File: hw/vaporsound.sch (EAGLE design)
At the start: 80 parts, among them Q1 BSS138, Q2 BSS138, X1 MSTBV2, X2 MSTBV2, X3 MSTBV2

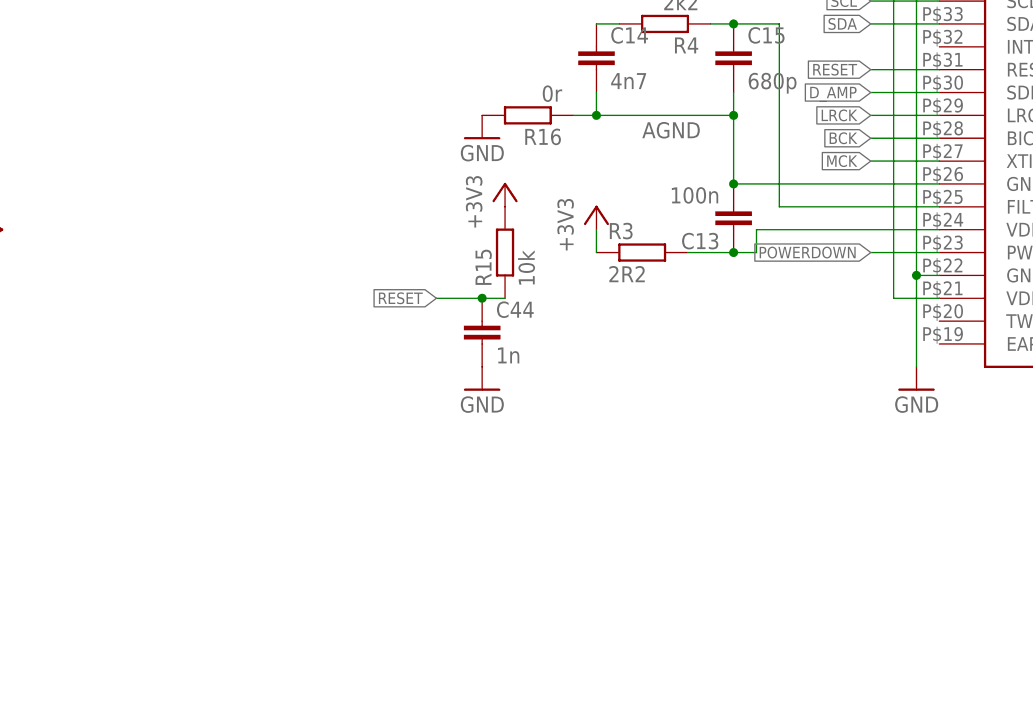
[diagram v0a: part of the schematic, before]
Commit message: Add pullup and pulldown STA350BW + minor layout fixes
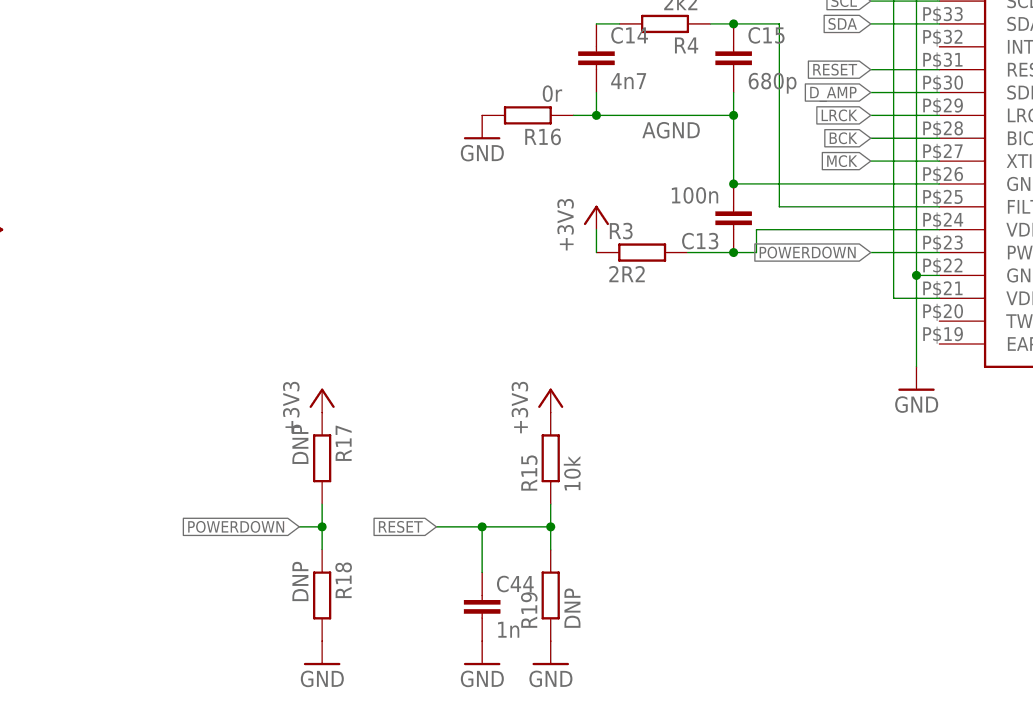
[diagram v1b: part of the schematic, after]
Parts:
- added R17, R18, R19: DNP, rcl:R-EU_R0603
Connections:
- net +3V3: now also R17.1
- net GND: now also R18.2, R19.1
- net POWERDOWN: now also R17.2, R18.1
- net RESET: now also R19.2
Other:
- moved on the sheet: C44, R15
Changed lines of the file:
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@@
 <?xml version="1.0" encoding="utf-8"?>
 <!DOCTYPE eagle SYSTEM "eagle.dtd">
-<eagle version="7.2.0">
+<eagle version="6.6.0">
 <drawing>
 <settings>
@@
 <part name="GND15" library="supply1" deviceset="GND" device=""/>
 <part name="L7" library="rcl" deviceset="R-EU_" device="R0805"/>
+<part name="R17" library="rcl" deviceset="R-EU_" device="R0603" value="DNP"/>
+<part name="R18" library="rcl" deviceset="R-EU_" device="R0603" value="DNP"/>
+<part name="+3V17" library="supply1" deviceset="+3V3" device=""/>
+<part name="GND17" library="supply1" deviceset="GND" device=""/>
+<part name="R19" library="rcl" deviceset="R-EU_" device="R0603" value="DNP"/>
+<part name="GND44" library="supply1" deviceset="GND" device=""/>
 </parts>
 <sheets>
@@
 <instance part="C42" gate="G$1" x="172.72" y="81.28"/>
 <instance part="C43" gate="G$1" x="165.1" y="81.28"/>
-<instance part="R15" gate="G$1" x="142.24" y="33.02" rot="R90"/>
-<instance part="+3V15" gate="G$1" x="142.24" y="40.64"/>
-<instance part="C44" gate="G$1" x="139.7" y="25.4"/>
-<instance part="GND40" gate="1" x="139.7" y="17.78" rot="MR0"/>
+<instance part="R15" gate="G$1" x="147.32" y="10.16" rot="R90"/>
+<instance part="+3V15" gate="G$1" x="147.32" y="17.78"/>
+<instance part="C44" gate="G$1" x="139.7" y="-5.08"/>
+<instance part="GND40" gate="1" x="139.7" y="-12.7" rot="MR0"/>
 <instance part="C45" gate="G$1" x="152.4" y="81.28"/>
 <instance part="+3V16" gate="G$1" x="152.4" y="86.36"/>
@@
 <instance part="GND15" gate="1" x="48.26" y="63.5"/>
 <instance part="L7" gate="G$1" x="-20.32" y="45.72"/>
+<instance part="R17" gate="G$1" x="121.92" y="10.16" rot="R270"/>
+<instance part="R18" gate="G$1" x="121.92" y="-5.08" rot="R270"/>
+<instance part="+3V17" gate="G$1" x="121.92" y="17.78"/>
+<instance part="GND17" gate="1" x="121.92" y="-12.7" rot="MR0"/>
+<instance part="R19" gate="G$1" x="147.32" y="-5.08" rot="R90"/>
+<instance part="GND44" gate="1" x="147.32" y="-12.7" rot="MR0"/>
 </instances>
 <busses>
@@
 <pinref part="GND15" gate="1" pin="GND"/>
 </segment>
+<segment>
+<pinref part="R18" gate="G$1" pin="2"/>
+<pinref part="GND17" gate="1" pin="GND"/>
+</segment>
+<segment>
+<pinref part="R19" gate="G$1" pin="1"/>
+<pinref part="GND44" gate="1" pin="GND"/>
+</segment>
 </net>
 <net name="V+" class="0">
@@
 <pinref part="+3V16" gate="G$1" pin="+3V3"/>
 </segment>
+<segment>
+<pinref part="R17" gate="G$1" pin="1"/>
+<pinref part="+3V17" gate="G$1" pin="+3V3"/>
+</segment>
 </net>
 <net name="ADC_VREF" class="0">
@@
 </segment>
 <segment>
-<wire x1="134.62" y1="27.94" x2="139.7" y2="27.94" width="0.1524" layer="91"/>
-<label x="134.62" y="27.94" size="1.27" layer="95" rot="R180" xref="yes"/>
+<label x="134.62" y="2.54" size="1.27" layer="95" rot="R180" xref="yes"/>
+<wire x1="134.62" y1="2.54" x2="139.7" y2="2.54" width="0.1524" layer="91"/>
+<pinref part="C44" gate="G$1" pin="1"/>
+<wire x1="139.7" y1="-2.54" x2="139.7" y2="2.54" width="0.1524" layer="91"/>
 <pinref part="R15" gate="G$1" pin="1"/>
-<pinref part="C44" gate="G$1" pin="1"/>
-<wire x1="139.7" y1="27.94" x2="142.24" y2="27.94" width="0.1524" layer="91"/>
-<junction x="139.7" y="27.94"/>
+<wire x1="139.7" y1="2.54" x2="147.32" y2="2.54" width="0.1524" layer="91"/>
+<wire x1="147.32" y1="2.54" x2="147.32" y2="5.08" width="0.1524" layer="91"/>
+<junction x="139.7" y="2.54"/>
+<pinref part="R19" gate="G$1" pin="2"/>
+<wire x1="147.32" y1="2.54" x2="147.32" y2="0" width="0.1524" layer="91"/>
+<junction x="147.32" y="2.54"/>
 </segment>
 </net>
@@
 <pinref part="U$1" gate="G$1" pin="PWRDN"/>
 <wire x1="190.5" y1="33.02" x2="182.88" y2="33.02" width="0.1524" layer="91"/>
-<label x="182.88" y="33.02" size="1.27" layer="95" rot="MR0" xref="yes"/>
+<label x="182.88" y="33.02" size="1.27" layer="95" rot="R180" xref="yes"/>
 </segment>
 <segment>
@@
 <label x="2.54" y="129.54" size="1.27" layer="95" rot="R180" xref="yes"/>
 </segment>
-</net>
+<segment>
+<pinref part="R18" gate="G$1" pin="1"/>
+<pinref part="R17" gate="G$1" pin="2"/>
+<wire x1="121.92" y1="5.08" x2="121.92" y2="2.54" width="0.1524" layer="91"/>
+<wire x1="121.92" y1="2.54" x2="121.92" y2="0" width="0.1524" layer="91"/>
+<junction x="121.92" y="2.54"/>
+<wire x1="121.92" y1="2.54" x2="119.38" y2="2.54" width="0.1524" layer="91"/>
+<label x="119.38" y="2.54" size="1.27" layer="95" rot="R180" xref="yes"/>
+</segment>
+</net>

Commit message: silkscreen
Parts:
- renumbered SV1 to DISP, SV2 to IN, U$4 to P9, X1 to SPKR1, X2 to SPKR2, X3 to PWR

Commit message: add inductor name to silkscreen
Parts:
- L1, L3, L4, L5: device srr1210-ind:L-EUSRR1210 -> custom-ind:L-EUSRR1210
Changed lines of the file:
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@@
 <part name="C15" library="rcl" deviceset="C-EU" device="C0603" value="680p"/>
 <part name="R4" library="rcl" deviceset="R-EU_" device="R0603" value="2k2"/>
-<part name="L1" library="srr1210-ind" deviceset="L-EU" device="SRR1210"/>
-<part name="L3" library="srr1210-ind" deviceset="L-EU" device="SRR1210"/>
-<part name="L4" library="srr1210-ind" deviceset="L-EU" device="SRR1210"/>
-<part name="L5" library="srr1210-ind" deviceset="L-EU" device="SRR1210"/>
 <part name="C16" library="rcl" deviceset="C-EU" device="C0603" value="330p"/>
 <part name="C17" library="rcl" deviceset="C-EU" device="C0603" value="330p"/>
@@
 <part name="P+9" library="supply1" deviceset="+24V" device=""/>
 <part name="C30" library="rcl" deviceset="C-EU" device="C0603" value="10n"/>
-<part name="L6" library="custom-ind" deviceset="L-EU" device="IHLP-3232DZ-11"/>
 <part name="D1" library="mircobuilder" deviceset="DIODE" device="SMA" value="B340A-13-F"/>
 <part name="GND23" library="supply1" deviceset="GND" device=""/>
@@
 <part name="R19" library="rcl" deviceset="R-EU_" device="R0603" value="DNP"/>
 <part name="GND44" library="supply1" deviceset="GND" device=""/>
+<part name="L1" library="custom-ind" deviceset="L-EU" device="SRR1210"/>
+<part name="L3" library="custom-ind" deviceset="L-EU" device="SRR1210"/>
+<part name="L4" library="custom-ind" deviceset="L-EU" device="SRR1210"/>
+<part name="L5" library="custom-ind" deviceset="L-EU" device="SRR1210"/>
+<part name="L6" library="custom-ind" deviceset="L-EU" device="IHLP-3232DZ-11"/>
 </parts>
 <sheets>
@@
 <instance part="C15" gate="G$1" x="167.64" y="55.88"/>
 <instance part="R4" gate="G$1" x="160.02" y="58.42" rot="R180"/>
-<instance part="L1" gate="G$1" x="279.4" y="17.78" rot="R90"/>
-<instance part="L3" gate="G$1" x="279.4" y="43.18" rot="R90"/>
-<instance part="L4" gate="G$1" x="279.4" y="45.72" rot="R90"/>
-<instance part="L5" gate="G$1" x="279.4" y="71.12" rot="R90"/>
 <instance part="C16" gate="G$1" x="271.78" y="53.34"/>
 <instance part="C17" gate="G$1" x="271.78" y="38.1"/>
@@
 <instance part="P+9" gate="1" x="-30.48" y="45.72" rot="R90"/>
 <instance part="C30" gate="G$1" x="50.8" y="40.64" rot="R90"/>
-<instance part="L6" gate="G$1" x="63.5" y="35.56" rot="R90"/>
 <instance part="D1" gate="G$1" x="53.34" y="30.48" rot="R90"/>
 <instance part="GND23" gate="1" x="53.34" y="22.86"/>
@@
 <instance part="R19" gate="G$1" x="147.32" y="-5.08" rot="R90"/>
 <instance part="GND44" gate="1" x="147.32" y="-12.7" rot="MR0"/>
+<instance part="L1" gate="G$1" x="279.4" y="17.78" rot="R90"/>
+<instance part="L3" gate="G$1" x="279.4" y="43.18" rot="R90"/>
+<instance part="L4" gate="G$1" x="279.4" y="45.72" rot="R90"/>
+<instance part="L5" gate="G$1" x="279.4" y="71.12" rot="R90"/>
+<instance part="L6" gate="G$1" x="63.5" y="35.56" rot="R90"/>
 </instances>
 <busses>
@@
 <wire x1="45.72" y1="45.72" x2="81.28" y2="45.72" width="0.1524" layer="91"/>
 <wire x1="81.28" y1="45.72" x2="81.28" y2="35.56" width="0.1524" layer="91"/>
-<pinref part="L6" gate="G$1" pin="2"/>
 <wire x1="68.58" y1="35.56" x2="71.12" y2="35.56" width="0.1524" layer="91"/>
 <junction x="81.28" y="35.56"/>
@@
 <wire x1="71.12" y1="33.02" x2="71.12" y2="35.56" width="0.1524" layer="91"/>
 <junction x="71.12" y="35.56"/>
+<pinref part="L6" gate="G$1" pin="2"/>
 </segment>
 <segment>
@@
 <wire x1="241.3" y1="53.34" x2="266.7" y2="53.34" width="0.1524" layer="91"/>
 <wire x1="266.7" y1="53.34" x2="266.7" y2="71.12" width="0.1524" layer="91"/>
-<pinref part="L5" gate="G$1" pin="1"/>
 <wire x1="266.7" y1="71.12" x2="271.78" y2="71.12" width="0.1524" layer="91"/>
 <pinref part="R5" gate="G$1" pin="2"/>
@@
 <wire x1="271.78" y1="68.58" x2="271.78" y2="71.12" width="0.1524" layer="91"/>
 <junction x="271.78" y="71.12"/>
+<pinref part="L5" gate="G$1" pin="1"/>
 </segment>
 </net>
@@
 <wire x1="266.7" y1="35.56" x2="266.7" y2="17.78" width="0.1524" layer="91"/>
 <wire x1="274.32" y1="17.78" x2="271.78" y2="17.78" width="0.1524" layer="91"/>
-<pinref part="L1" gate="G$1" pin="1"/>
 <pinref part="R6" gate="G$1" pin="1"/>
 <wire x1="271.78" y1="17.78" x2="266.7" y2="17.78" width="0.1524" layer="91"/>
 <wire x1="271.78" y1="20.32" x2="271.78" y2="17.78" width="0.1524" layer="91"/>
 <junction x="271.78" y="17.78"/>
+<pinref part="L1" gate="G$1" pin="1"/>
 </segment>
 </net>
@@
 <pinref part="C18" gate="G$1" pin="1"/>
 <wire x1="287.02" y1="66.04" x2="287.02" y2="71.12" width="0.1524" layer="91"/>
-<pinref part="L5" gate="G$1" pin="2"/>
 <wire x1="287.02" y1="71.12" x2="284.48" y2="71.12" width="0.1524" layer="91"/>
 <wire x1="287.02" y1="71.12" x2="320.04" y2="71.12" width="0.1524" layer="91"/>
@@
 <junction x="320.04" y="71.12"/>
 <pinref part="SPKR2" gate="-2" pin="1"/>
+<pinref part="L5" gate="G$1" pin="2"/>
 </segment>
 </net>
@@
 <net name="SPKR2A" class="0">
 <segment>
-<pinref part="L4" gate="G$1" pin="2"/>
 <wire x1="284.48" y1="45.72" x2="287.02" y2="45.72" width="0.1524" layer="91"/>
 <pinref part="C20" gate="G$1" pin="1"/>
@@
 <junction x="320.04" y="45.72"/>
 <pinref part="SPKR2" gate="-1" pin="1"/>
+<pinref part="L4" gate="G$1" pin="2"/>
 </segment>
 </net>
@@
 <segment>
 <pinref part="U$1" gate="G$1" pin="OUT2A"/>
-<pinref part="L4" gate="G$1" pin="1"/>
 <wire x1="241.3" y1="45.72" x2="271.78" y2="45.72" width="0.1524" layer="91"/>
 <pinref part="C16" gate="G$1" pin="2"/>
@@
 <wire x1="271.78" y1="48.26" x2="271.78" y2="45.72" width="0.1524" layer="91"/>
 <junction x="271.78" y="45.72"/>
+<pinref part="L4" gate="G$1" pin="1"/>
 </segment>
 </net>
@@
 <segment>
 <pinref part="U$1" gate="G$1" pin="OUT1B"/>
-<pinref part="L3" gate="G$1" pin="1"/>
 <wire x1="241.3" y1="43.18" x2="271.78" y2="43.18" width="0.1524" layer="91"/>
 <pinref part="C17" gate="G$1" pin="1"/>
@@
 <wire x1="271.78" y1="43.18" x2="271.78" y2="40.64" width="0.1524" layer="91"/>
 <junction x="271.78" y="43.18"/>
+<pinref part="L3" gate="G$1" pin="1"/>
 </segment>
 </net>
 <net name="SPKR1B" class="0">
 <segment>
-<pinref part="L3" gate="G$1" pin="2"/>
 <pinref part="C22" gate="G$1" pin="1"/>
 <wire x1="284.48" y1="43.18" x2="287.02" y2="43.18" width="0.1524" layer="91"/>
@@
 <junction x="320.04" y="43.18"/>
 <pinref part="SPKR1" gate="-2" pin="1"/>
+<pinref part="L3" gate="G$1" pin="2"/>
 </segment>
 </net>
 <net name="SPKR1A" class="0">
 <segment>
-<pinref part="L1" gate="G$1" pin="2"/>
 <pinref part="C24" gate="G$1" pin="1"/>
 <wire x1="284.48" y1="17.78" x2="287.02" y2="17.78" width="0.1524" layer="91"/>
@@
 <junction x="320.04" y="17.78"/>
 <pinref part="SPKR1" gate="-1" pin="1"/>
+<pinref part="L1" gate="G$1" pin="2"/>
 </segment>
 </net>
@@
 <wire x1="53.34" y1="35.56" x2="55.88" y2="35.56" width="0.1524" layer="91"/>
 <wire x1="55.88" y1="35.56" x2="55.88" y2="40.64" width="0.1524" layer="91"/>
-<pinref part="L6" gate="G$1" pin="1"/>
 <wire x1="58.42" y1="35.56" x2="55.88" y2="35.56" width="0.1524" layer="91"/>
 <junction x="55.88" y="35.56"/>
@@
 <wire x1="53.34" y1="33.02" x2="53.34" y2="35.56" width="0.1524" layer="91"/>
 <junction x="53.34" y="35.56"/>
-</segment>
-</net>
+<pinref part="L6" gate="G$1" pin="1"/>
+</segment>
+</net>

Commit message: move reset to different bbb pin and remove pull-down resistor
reset of the sta350 is now connected to a pin with pull-up on the bbb instead of one with a pull-down
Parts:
- removed R19: DNP, rcl:R-EU_R0603
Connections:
- net GND: no longer R19.1
- net RESET: now also P9.13; no longer P9.15, R19.2
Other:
- moved on the sheet: C30, C31, C32, C33, C34, C35, C36, C44, D1, L6, L7, PWR-1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

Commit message: add 1wire temperature sensor + some thermal optimizations
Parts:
- added R19: 4k7, rcl:R-EU_R0603
- added TEMP: (no value), con-lstb:MA03-1
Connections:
- new net 1WIRE: P9.12, R19.1, TEMP.2
- net +3V3: now also R19.2, TEMP.3
- net GND: now also TEMP.1
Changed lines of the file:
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@@
 <part name="L5" library="custom-ind" deviceset="L-EU" device="SRR1210"/>
 <part name="L6" library="custom-ind" deviceset="L-EU" device="IHLP-3232DZ-11"/>
+<part name="TEMP" library="con-lstb" deviceset="MA03-1" device=""/>
+<part name="GND44" library="supply1" deviceset="GND" device=""/>
+<part name="+3V18" library="supply1" deviceset="+3V3" device=""/>
+<part name="+3V19" library="supply1" deviceset="+3V3" device=""/>
+<part name="R19" library="rcl" deviceset="R-EU_" device="R0603" value="4k7"/>
 </parts>
 <sheets>
@@
 <instance part="L5" gate="G$1" x="279.4" y="71.12" rot="R90"/>
 <instance part="L6" gate="G$1" x="93.98" y="43.18" rot="R90"/>
+<instance part="TEMP" gate="G$1" x="325.12" y="111.76" rot="R180"/>
+<instance part="GND44" gate="1" x="314.96" y="114.3" rot="MR90"/>
+<instance part="+3V18" gate="G$1" x="307.34" y="127"/>
+<instance part="+3V19" gate="G$1" x="314.96" y="109.22" rot="R90"/>
+<instance part="R19" gate="G$1" x="307.34" y="119.38" rot="R90"/>
 </instances>
 <busses>
@@
 <pinref part="GND17" gate="1" pin="GND"/>
 </segment>
+<segment>
+<pinref part="TEMP" gate="G$1" pin="1"/>
+<pinref part="GND44" gate="1" pin="GND"/>
+</segment>
 </net>
 <net name="V+" class="0">
@@
 <pinref part="+3V17" gate="G$1" pin="+3V3"/>
 </segment>
+<segment>
+<pinref part="TEMP" gate="G$1" pin="3"/>
+<pinref part="+3V19" gate="G$1" pin="+3V3"/>
+</segment>
+<segment>
+<pinref part="R19" gate="G$1" pin="2"/>
+<pinref part="+3V18" gate="G$1" pin="+3V3"/>
+</segment>
 </net>
 <net name="ADC_VREF" class="0">
@@
 </segment>
 </net>
+<net name="1WIRE" class="0">
+<segment>
+<pinref part="TEMP" gate="G$1" pin="2"/>
+<wire x1="317.5" y1="111.76" x2="307.34" y2="111.76" width="0.1524" layer="91"/>
+<label x="304.8" y="111.76" size="1.27" layer="95" rot="R180" xref="yes"/>
+<pinref part="R19" gate="G$1" pin="1"/>
+<wire x1="307.34" y1="111.76" x2="304.8" y2="111.76" width="0.1524" layer="91"/>
+<wire x1="307.34" y1="114.3" x2="307.34" y2="111.76" width="0.1524" layer="91"/>
+<junction x="307.34" y="111.76"/>
+</segment>
+<segment>
+<pinref part="P9" gate="G$1" pin="12"/>
+<wire x1="25.4" y1="144.78" x2="33.02" y2="144.78" width="0.1524" layer="91"/>
+<label x="33.02" y="144.78" size="1.27" layer="95" xref="yes"/>
+</segment>
+</net>

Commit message: add missing values
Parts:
- C10, C9: value (none) -> DNP
- C2, C4, C6: value (none) -> 10u
- L1, L3, L4, L5, L6: value (none) -> 22u
- L2, L7: value (none) -> 1uH
- R1, R2: value (none) -> 0R
- R16: value 0r -> 0R
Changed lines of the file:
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@@
 <part name="GND5" library="supply1" deviceset="GND" device=""/>
 <part name="GND6" library="supply1" deviceset="GND" device=""/>
-<part name="L2" library="rcl" deviceset="R-EU_" device="R0805"/>
+<part name="L2" library="rcl" deviceset="R-EU_" device="R0805" value="1uH"/>
 <part name="P+1" library="supply1" deviceset="V+" device=""/>
 <part name="P+2" library="supply1" deviceset="V+" device=""/>
@@
 <part name="+3V1" library="supply1" deviceset="+3V3" device=""/>
 <part name="C1" library="rcl" deviceset="C-EU" device="C0603" value="100n"/>
-<part name="C2" library="rcl" deviceset="C-EU" device="C0805"/>
+<part name="C2" library="rcl" deviceset="C-EU" device="C0805" value="10u"/>
 <part name="P+6" library="supply1" deviceset="V+" device=""/>
 <part name="GND7" library="supply1" deviceset="GND" device=""/>
 <part name="GND8" library="supply1" deviceset="GND" device=""/>
 <part name="C3" library="rcl" deviceset="C-EU" device="C0603" value="100n"/>
-<part name="C4" library="rcl" deviceset="C-EU" device="C0805"/>
+<part name="C4" library="rcl" deviceset="C-EU" device="C0805" value="10u"/>
 <part name="GND9" library="supply1" deviceset="GND" device=""/>
 <part name="GND10" library="supply1" deviceset="GND" device=""/>
 <part name="C5" library="rcl" deviceset="C-EU" device="C0603" value="100n"/>
-<part name="C6" library="rcl" deviceset="C-EU" device="C0805"/>
+<part name="C6" library="rcl" deviceset="C-EU" device="C0805" value="10u"/>
 <part name="GND11" library="supply1" deviceset="GND" device=""/>
 <part name="GND12" library="supply1" deviceset="GND" device=""/>
@@
 <part name="C7" library="rcl" deviceset="CPOL-EU" device="E2-5" value="1u"/>
 <part name="C8" library="rcl" deviceset="CPOL-EU" device="E2-5" value="1u"/>
-<part name="C9" library="rcl" deviceset="C-EU" device="C0603"/>
-<part name="C10" library="rcl" deviceset="C-EU" device="C0603"/>
+<part name="C9" library="rcl" deviceset="C-EU" device="C0603" value="DNP"/>
+<part name="C10" library="rcl" deviceset="C-EU" device="C0603" value="DNP"/>
 <part name="GND13" library="supply1" deviceset="GND" device=""/>
 <part name="GND14" library="supply1" deviceset="GND" device=""/>
-<part name="R1" library="rcl" deviceset="R-EU_" device="R0603"/>
-<part name="R2" library="rcl" deviceset="R-EU_" device="R0603"/>
+<part name="R1" library="rcl" deviceset="R-EU_" device="R0603" value="0R"/>
+<part name="R2" library="rcl" deviceset="R-EU_" device="R0603" value="0R"/>
 <part name="+3V5" library="supply1" deviceset="+3V3" device=""/>
 <part name="C11" library="rcl" deviceset="C-EU" device="C0603" value="100n"/>
@@
 <part name="+3V16" library="supply1" deviceset="+3V3" device=""/>
 <part name="GND43" library="supply1" deviceset="GND" device=""/>
-<part name="R16" library="rcl" deviceset="R-EU_" device="R0603" value="0r"/>
+<part name="R16" library="rcl" deviceset="R-EU_" device="R0603" value="0R"/>
 <part name="GND16" library="supply1" deviceset="GND" device=""/>
 <part name="SPKR1" library="con-phoenix-508" deviceset="MSTBV2" device=""/>
@@
 <part name="P+21" library="supply1" deviceset="+24V" device=""/>
 <part name="GND15" library="supply1" deviceset="GND" device=""/>
-<part name="L7" library="rcl" deviceset="R-EU_" device="R0805"/>
+<part name="L7" library="rcl" deviceset="R-EU_" device="R0805" value="1uH"/>
 <part name="R17" library="rcl" deviceset="R-EU_" device="R0603" value="DNP"/>
 <part name="R18" library="rcl" deviceset="R-EU_" device="R0603" value="DNP"/>
 <part name="+3V17" library="supply1" deviceset="+3V3" device=""/>
 <part name="GND17" library="supply1" deviceset="GND" device=""/>
-<part name="L1" library="custom-ind" deviceset="L-EU" device="SRR1210"/>
-<part name="L3" library="custom-ind" deviceset="L-EU" device="SRR1210"/>
-<part name="L4" library="custom-ind" deviceset="L-EU" device="SRR1210"/>
-<part name="L5" library="custom-ind" deviceset="L-EU" device="SRR1210"/>
-<part name="L6" library="custom-ind" deviceset="L-EU" device="IHLP-3232DZ-11"/>
+<part name="L1" library="custom-ind" deviceset="L-EU" device="SRR1210" value="22u"/>
+<part name="L3" library="custom-ind" deviceset="L-EU" device="SRR1210" value="22u"/>
+<part name="L4" library="custom-ind" deviceset="L-EU" device="SRR1210" value="22u"/>
+<part name="L5" library="custom-ind" deviceset="L-EU" device="SRR1210" value="22u"/>
+<part name="L6" library="custom-ind" deviceset="L-EU" device="IHLP-3232DZ-11" value="22u"/>
 <part name="TEMP" library="con-lstb" deviceset="MA03-1" device=""/>
 <part name="GND44" library="supply1" deviceset="GND" device=""/>
